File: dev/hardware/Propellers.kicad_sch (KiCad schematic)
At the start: 25 parts, among them J201 CPU PGMR, J202 GPU PGMR, J203 SPARE GPU HDR, J204 SPARE CPU HDR, SW201 CPU ~{RES}, SW202 GPU ~{RES}, SW203 DEBUG, U1 P8X32A-D40, Y1 6.5MHz

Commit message: Finished draft PCB
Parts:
- removed J203: SPARE GPU HDR, Connector_PinHeader_2.54mm:PinHeader_2x05_P2.54mm_Vertical, symbol Connector_Generic:Conn_02x05_Top_Bottom
- added J203: SPARE GPU HDR, Connector_PinHeader_2.54mm:PinHeader_2x04_P2.54mm_Vertical, symbol Connector_Generic:Conn_02x04_Top_Bottom
- J204: footprint Connector_PinHeader_2.54mm:PinHeader_2x08_P2.54mm_Vertical -> Connector_PinHeader_2.54mm:PinHeader_2x07_P2.54mm_Vertical; symbol Connector_Generic:Conn_02x08_Top_Bottom -> Connector_Generic:Conn_02x07_Top_Bottom
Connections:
- net GPU_SPARE_8 is gone; now on net GPU_SPARE_6: U1.7 (P6)
- net GPU_SPARE_9 is gone; now on net GPU_SPARE_7: U1.8 (P7)
- net CPU_SPARE_1: now also U1.4 (P3); no longer U1.33 (P24)
- net CPU_SPARE_10: now also U1.17 (P12); no longer U1.15 (P10)
- net CPU_SPARE_11: now also U1.18 (P13); no longer U1.16 (P11)
- net CPU_SPARE_12: now also U1.19 (P14); no longer U1.17 (P12)
- net CPU_SPARE_13: now also U1.20 (P15); no longer U1.18 (P13)
- net CPU_SPARE_2: now also U1.5 (P4); no longer U1.34 (P25)
- net CPU_SPARE_3: now also U1.6 (P5); no longer U1.4 (P3)
- net CPU_SPARE_4: now also U1.7 (P6); no longer U1.5 (P4)
- net CPU_SPARE_5: now also U1.8 (P7); no longer U1.6 (P5)
- net CPU_SPARE_6: now also U1.13 (P8); no longer U1.7 (P6)
- net CPU_SPARE_7: now also U1.14 (P9); no longer U1.8 (P7)
- net CPU_SPARE_8: now also U1.15 (P10); no longer U1.13 (P8)
- net CPU_SPARE_9: now also U1.16 (P11); no longer U1.14 (P9)
- net GPU_SPARE_1: now also U1.2 (P1), J203.1 (Pin_1); no longer U1.35 (P26)
- net GPU_SPARE_2: now also U1.3 (P2), J203.2 (Pin_2); no longer U1.36 (P27)
- net GPU_SPARE_3: now also U1.4 (P3), J203.3 (Pin_3); no longer U1.2 (P1)
- net GPU_SPARE_4: now also U1.5 (P4), J203.4 (Pin_4); no longer U1.3 (P2)
- net GPU_SPARE_5: now also U1.6 (P5), J203.5 (Pin_5); no longer U1.4 (P3)
- net GPU_SPARE_6: now also J203.6 (Pin_6); no longer U1.5 (P4)
- net GPU_SPARE_7: now also J203.7 (Pin_7); no longer U1.6 (P5)
- net CPU_SPARE_14: no longer names the net of J204.14 (Pin_14)
- net CPU_SPARE_14: no longer U1.19 (P14)
- removed net CPU_SPARE_15: J204.15 (Pin_15), U1.20 (P15)
- no-connect marks 2 -> 6

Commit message: Finalized optimized board layout
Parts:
- removed R1 (x8): 200, Resistor_THT:R_Axial_DIN0207_L6.3mm_D2.5mm_P10.16mm_Horizontal, symbol Device:R
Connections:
- net GPU_DAT_1 is gone; now on net GFX_DAT_1: U1.13 (P8)
- net GPU_DAT_2 is gone; now on net GFX_DAT_2: U1.14 (P9)
- net GPU_DAT_3 is gone; now on net GFX_DAT_3: U1.15 (P10)
- net GPU_DAT_4 is gone; now on net GFX_DAT_4: U1.16 (P11)
- net GPU_DAT_5 is gone; now on net GFX_DAT_5: U1.17 (P12)
- net GPU_DAT_6 is gone; now on net GFX_DAT_6: U1.18 (P13)
- net GPU_DAT_7 is gone; now on net GFX_DAT_7: U1.19 (P14)
- net GPU_DAT_8 is gone; now on net GFX_DAT_8: U1.20 (P15)
- net CPU_DAT_1 renamed GFX_DAT_1
- net CPU_DAT_2 renamed GFX_DAT_2
- net CPU_DAT_3 renamed GFX_DAT_3
- net CPU_DAT_4 renamed GFX_DAT_4
- net CPU_DAT_5 renamed GFX_DAT_5
- net CPU_DAT_6 renamed GFX_DAT_6
- net CPU_DAT_7 renamed GFX_DAT_7
- net CPU_DAT_8 renamed GFX_DAT_8

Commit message: Finalized review schematic & pcb
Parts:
- removed C1 (x4): 0.1u, Capacitor_THT:C_Disc_D3.4mm_W2.1mm_P2.50mm, symbol Device:C
- added C1 (x4): 0.1u, Capacitor_THT:C_Disc_D3.4mm_W2.1mm_P2.50mm, symbol Device:C
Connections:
- net +3.3V: now also U1.12 (VDD), U1.12 (VDD), U1.32 (VDD), U1.32 (VDD), C1.2, C1.2, C1.2, C1.2
- net GND: now also C1.1, C1.1, C1.1, C1.1
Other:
- moved on the sheet: J201, J202, J203, J204, R1, SW201, SW202, SW203, U1, Y1

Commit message: Thicc-traced VGA sig test - REVERT HERE
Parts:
- renumbered C1 to C?, J204 to J202, J202 to J203, J203 to J204, R1 to R?, SW203 to SW202, SW202 to SW203, U1 to U?, Y1 to Y?

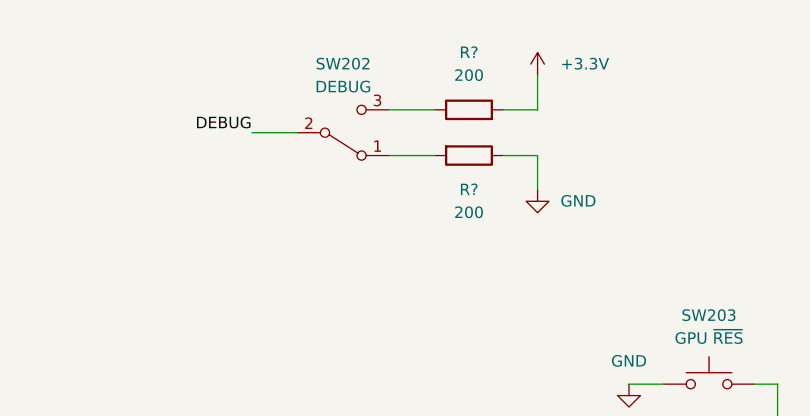
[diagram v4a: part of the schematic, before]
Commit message: Implemented review changes - missing reverse polarity protection
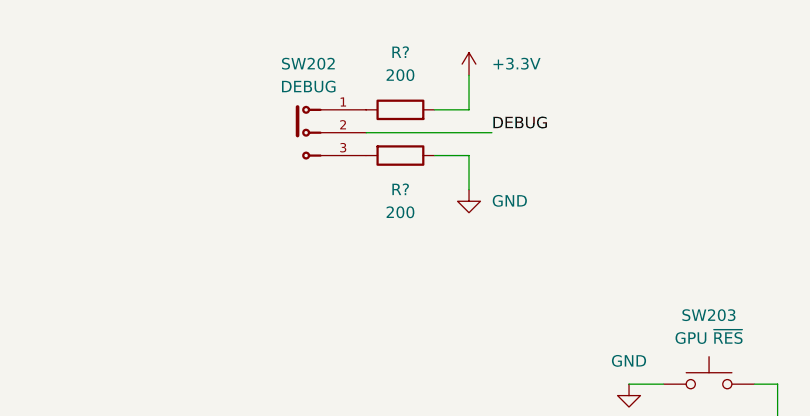
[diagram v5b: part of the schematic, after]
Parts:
- removed C?: 0.1u, Capacitor_THT:C_Disc_D3.4mm_W2.1mm_P2.50mm, symbol Device:C
- added C?: 0.1u, Capacitor_THT:C_Disc_D3.4mm_W2.1mm_P2.50mm, symbol Device:C
- SW202: footprint Button_Switch_THT:SW_Slide_1P2T_CK_OS102011MS2Q -> jcap-footprints:SW_1825159-1; symbol Switch:SW_SPDT -> jcap-symbols:1825159-1
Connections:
- net +3.3V: now also C?.2
- net GND: now also C?.1
- net at SW202.1: now also R?.1; no longer R?.2
- net at SW202.3: now also R?.2; no longer R?.1
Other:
- moved on the sheet: R?

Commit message: Finalized dev board administrivia
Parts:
- removed C? (x3): 0.1u, Capacitor_THT:C_Disc_D3.4mm_W2.1mm_P2.50mm, symbol Device:C
- removed R?: 200, Resistor_THT:R_Axial_DIN0207_L6.3mm_D2.5mm_P10.16mm_Horizontal, symbol Device:R
- removed Y?: 6.5MHz, Crystal:Crystal_HC49-U_Vertical, symbol Device:Crystal
- added C? (x3): 0.1u, Capacitor_THT:C_Disc_D3.4mm_W2.1mm_P2.50mm, symbol Device:C
- added R?: 10K, Resistor_THT:R_Axial_DIN0207_L6.3mm_D2.5mm_P10.16mm_Horizontal, symbol Device:R
- added Y?: 6.5MHz, Crystal:Crystal_HC49-U_Vertical, symbol Device:Crystal
- C?, J201, J203: Part (none) -> K104K15X7RF5TL2
- J202: Part (none) -> PH2-14-UA
- J204: Part (none) -> PH2-08-UA
- R?: value 200 -> 10K; Part (none) -> RNF14FTD10K0
- SW201, SW203: Part (none) -> B3F-1002
- SW202: Part (none) -> EG1218
- U? (x2): value P8X32A-D40 -> P8X32A; Part (none) -> P8X32A-D40
- Y?: Part (none) -> ECS-65-20-4X
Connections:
- net +3.3V: now also C?.2, C?.2, C?.2
- net GND: now also C?.1, C?.1, C?.1, R?.2
- net at SW202.3: now also R?.1
- net at U?.31 (XO): now also Y?.1
- net at U?.30 (XI): now also Y?.2
